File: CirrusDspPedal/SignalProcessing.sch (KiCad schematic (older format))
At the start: 19 parts, among them J3 Conn_02x05_Odd_Even, J8 Conn_01x04, U7 STM32F405RGTx

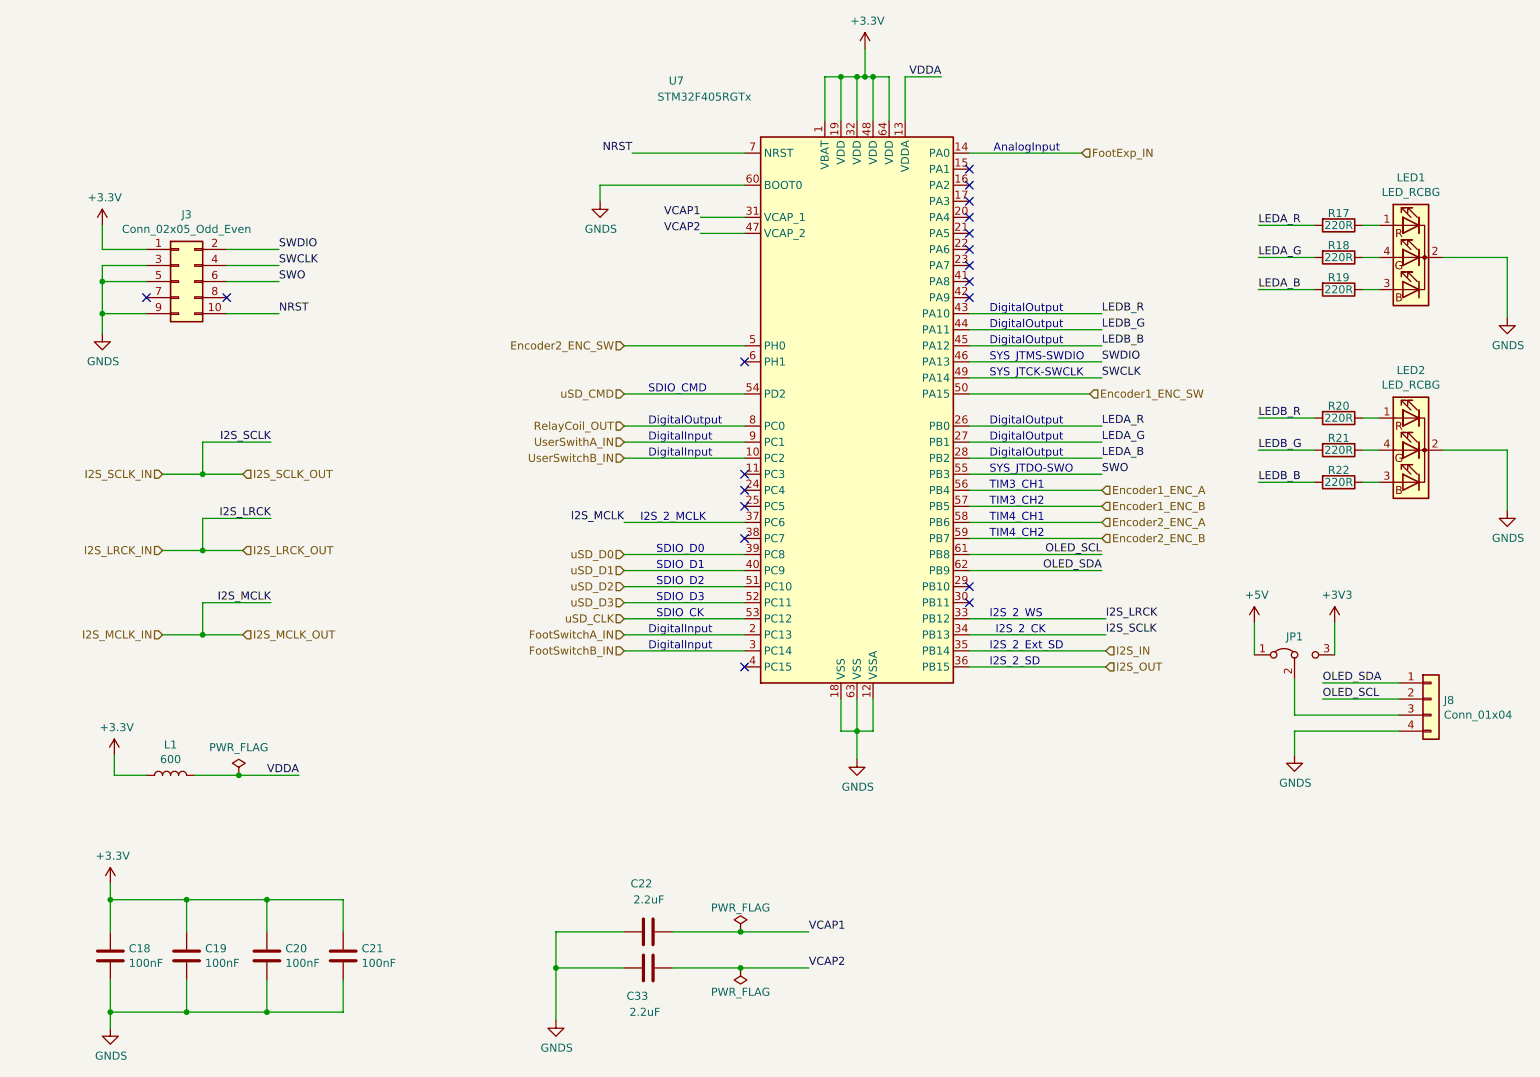
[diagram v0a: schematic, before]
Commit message: updated revb
- Moved THT components to improve UX layout
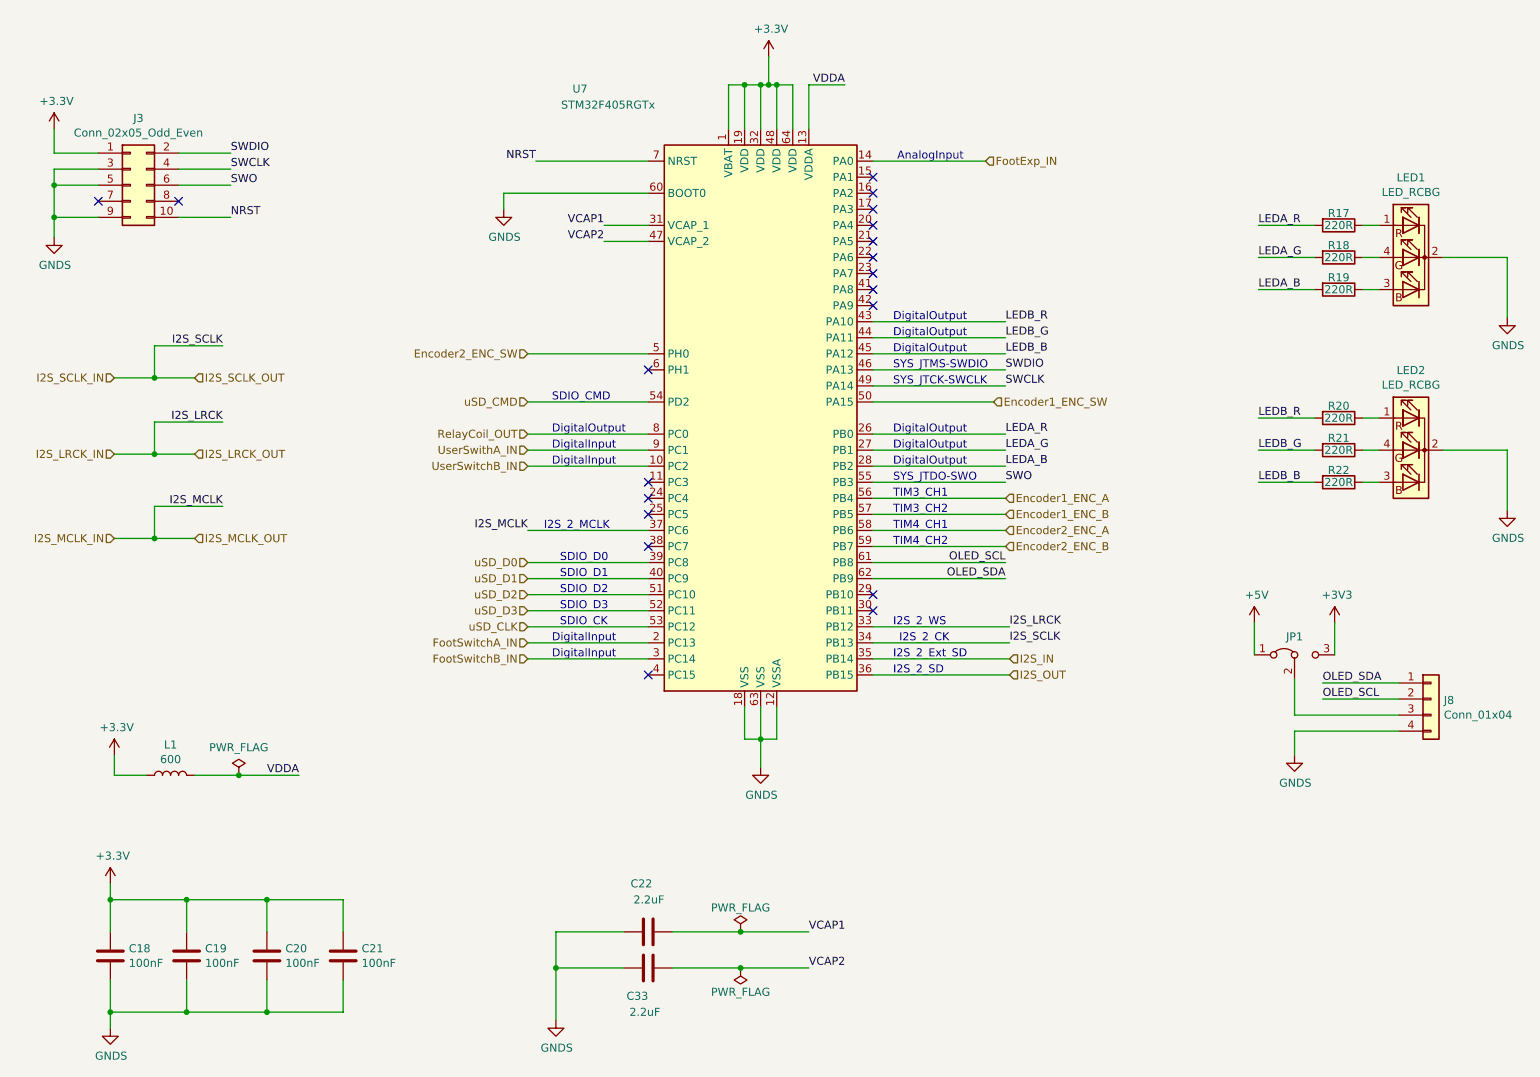
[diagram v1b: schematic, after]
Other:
- moved on the sheet: J3, U7
